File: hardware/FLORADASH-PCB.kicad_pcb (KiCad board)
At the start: 4 copper layers, 139.5 x 50.9 mm, 87 parts, among them IC1 LM66200DRLR, J1 USB_C_Receptacle_USB2.0_16P, J2 Conn_01x04_Pin, J3 Conn_02x04_Top_Bottom, Q1 FS8205, Q2 FS8205, SW1 SW_Push, SW2 SW_Push, U1 TP4056-42-ESOP8, U2 USBLC6-2SC6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

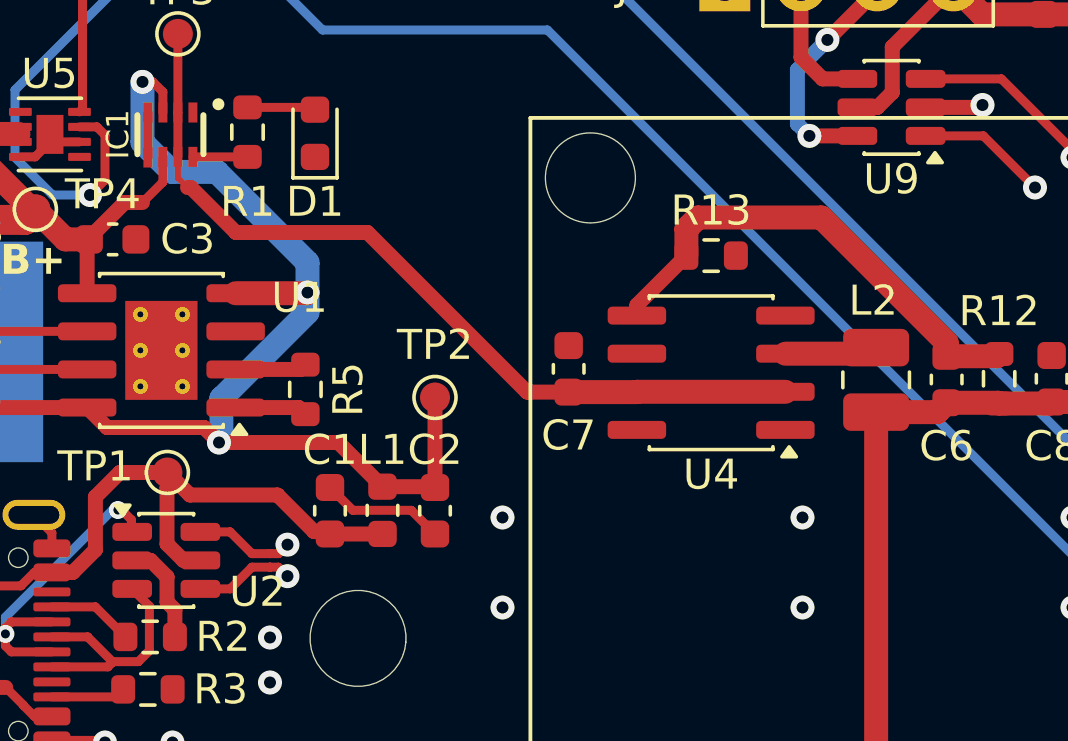
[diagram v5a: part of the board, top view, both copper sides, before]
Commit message: Finished routing PCB
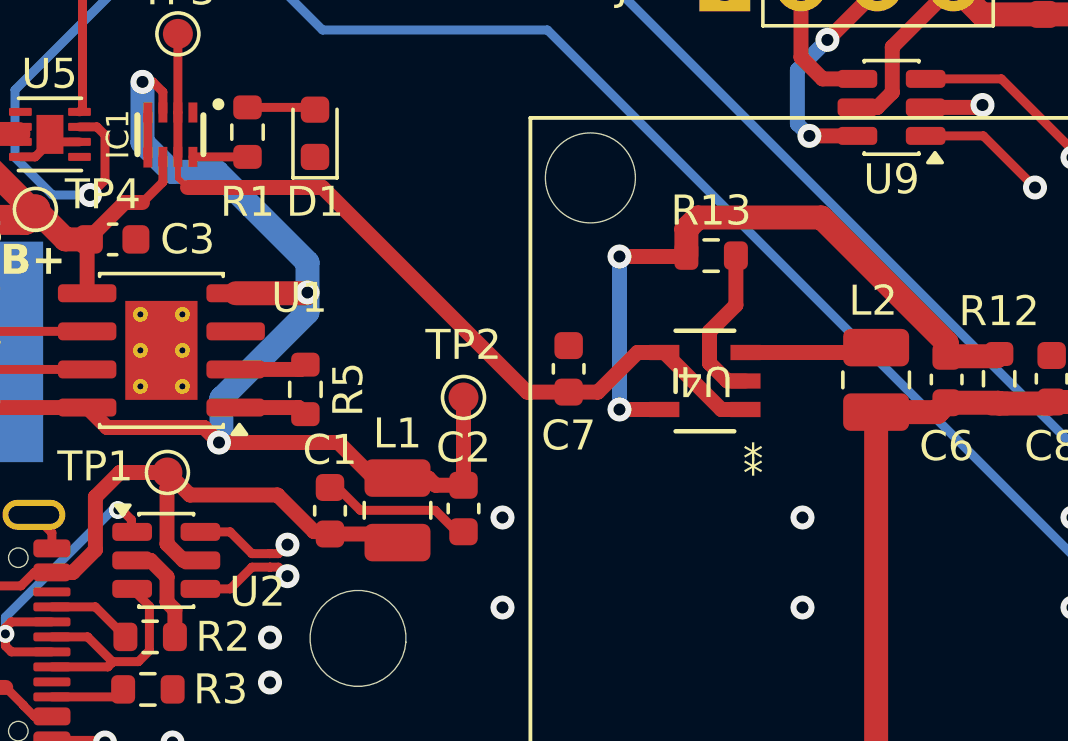
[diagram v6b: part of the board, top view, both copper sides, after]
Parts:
- L1: value 2n2 -> 2u2; footprint Inductor_SMD:L_0603_1608Metric -> Inductor_SMD:L_1008_2520Metric
- U4: value MT3420SP -> ~; footprint Package_SO:SOIC-8_3.9x4.9mm_P1.27mm -> SY8089BAAC:SY8089AAAC_SGY
- moved C2 0.95 mm to (124.7, 109.7)
- moved TP2 0.95 mm to (124.7, 106.0)
- moved L1 0.50 mm to (122.5, 109.8)
- moved U4 0.34 mm to (132.7, 105.4)
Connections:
- U4 pad 1: unconnected-(U4-NC-Pad1) -> battery/usb
- U4 pad 2: battery/usb -> GND
- U4 pad 4: GND -> battery/usb
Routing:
- net GND: track 37.2 -> 43.5 mm
- net Net-(U4-FB): track 16.4 -> 22.5 mm, vias 0 -> 2
- net Net-(U4-LX): track 3.11 -> 4.42 mm
- net +5V_FILT: track 47.6 -> 48.4 mm
- net +5V: track 26.6 -> 27.2 mm
